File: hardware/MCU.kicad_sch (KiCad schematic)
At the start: 7 parts, among them J1 TC2030-SWD, U2 STM32G0C1KETxN

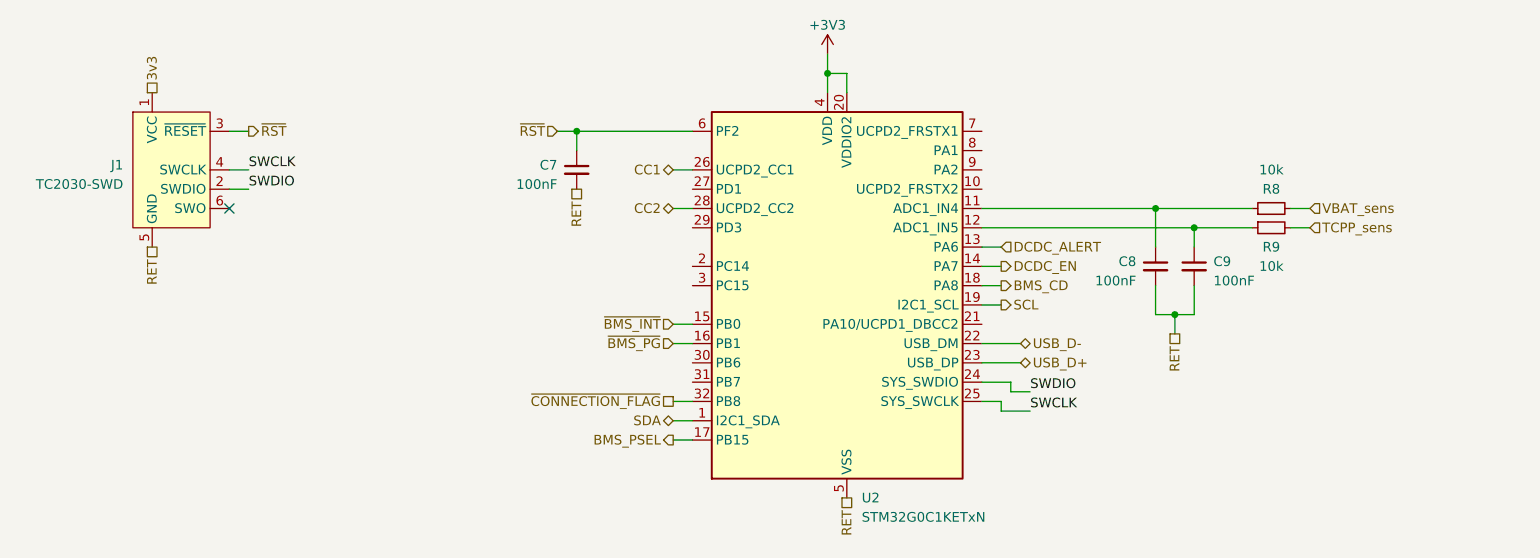
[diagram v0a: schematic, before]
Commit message: Some routing and pinout changes
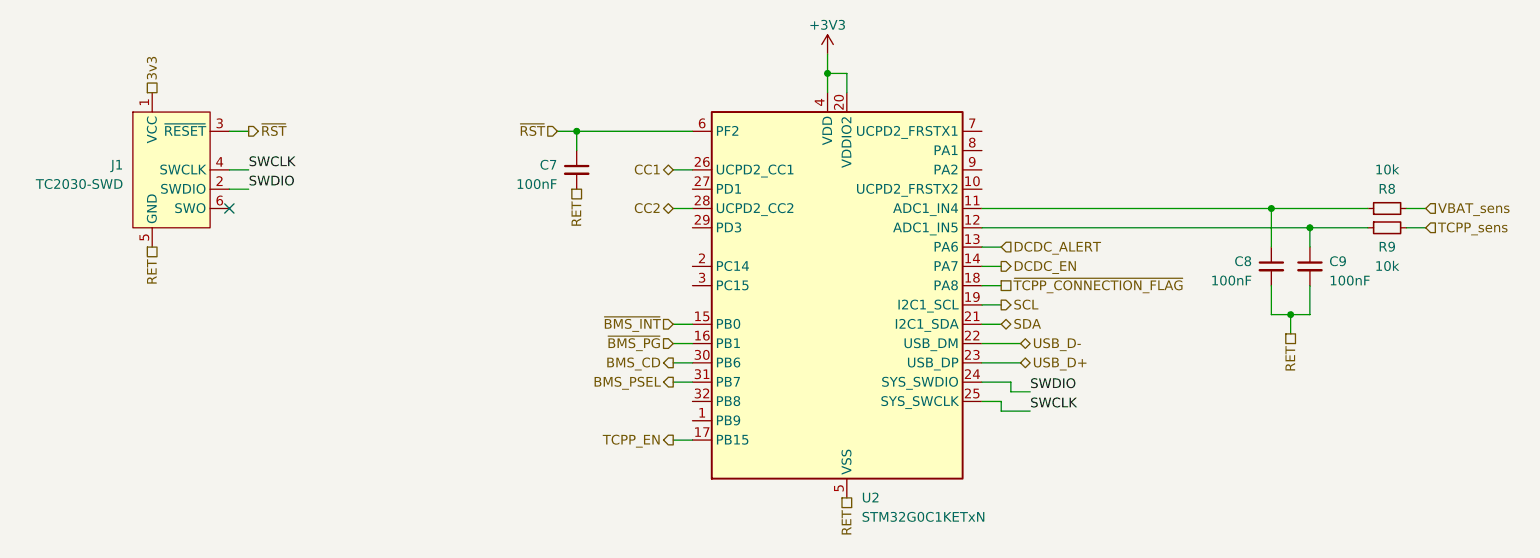
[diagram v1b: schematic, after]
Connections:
- net BMS_CD: now also U2.30 (PB6); no longer U2.18 (PA8)
- net BMS_PSEL: now also U2.31 (PB7); no longer U2.17 (PB15)
- net SDA: now also U2.21 (PA10/UCPD1_DBCC2); no longer U2.1 (PB9)
- net ~{CONNECTION_FLAG}: no longer names the net of U2.32 (PB8)
- new net TCPP_EN: U2.17 (PB15)
- new net ~{TCPP_CONNECTION_FLAG}: U2.18 (PA8)
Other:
- moved on the sheet: C8, C9, R8, R9
